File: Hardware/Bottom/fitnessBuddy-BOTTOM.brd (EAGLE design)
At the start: 160 x 100 mm, 31 parts, among them U1 AD5242-SO16

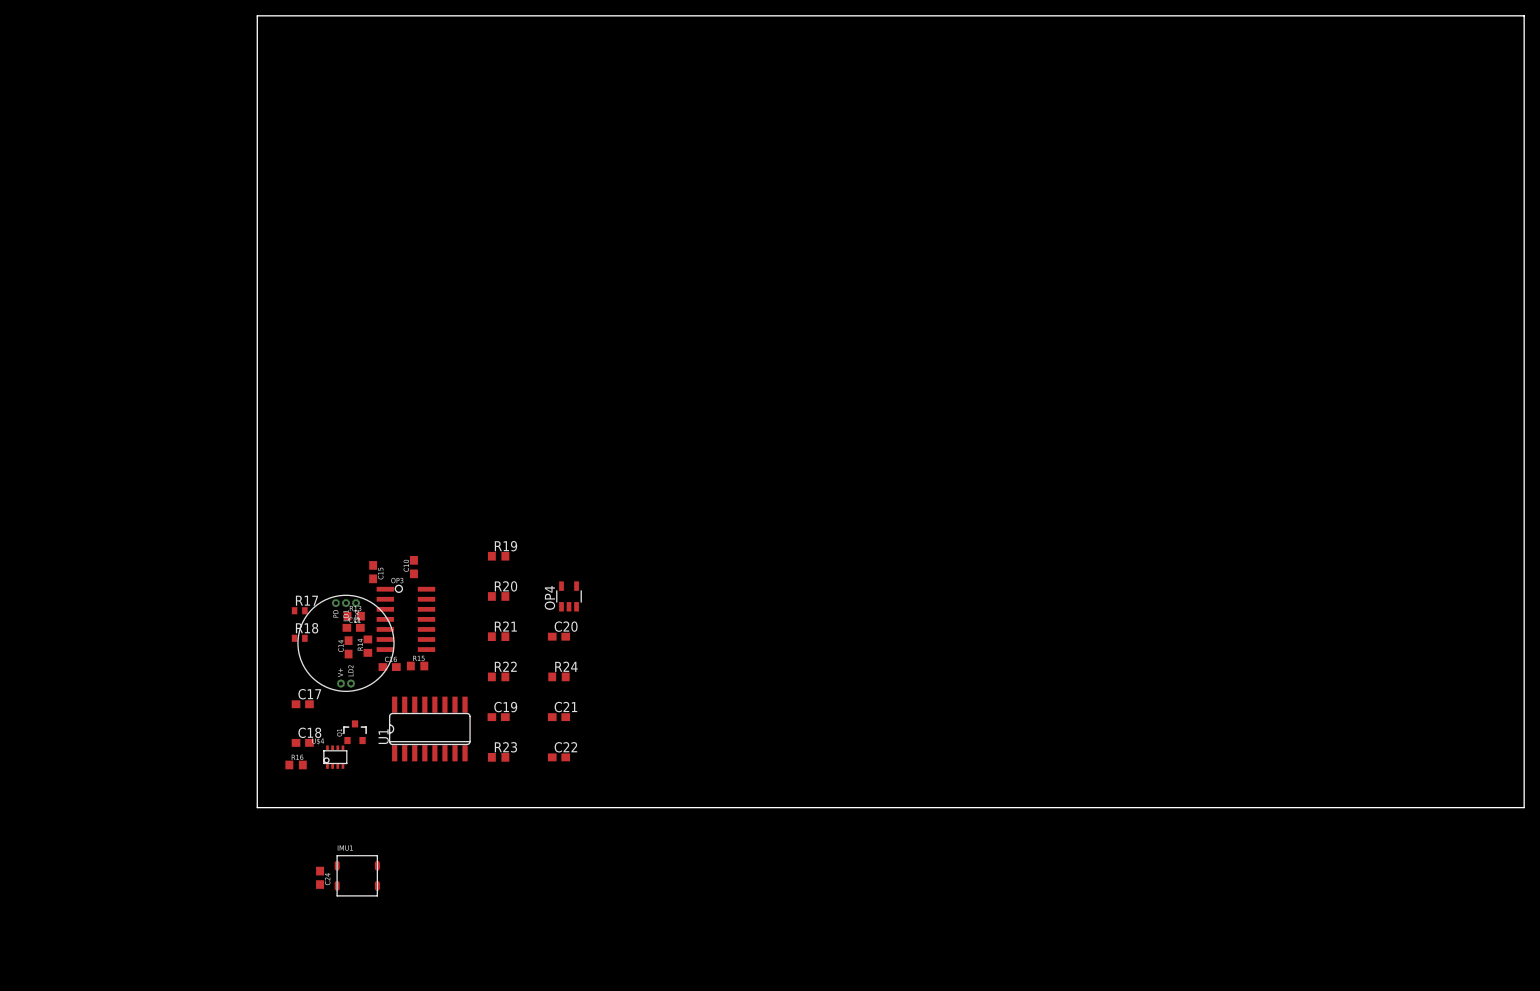
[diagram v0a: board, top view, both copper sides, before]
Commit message: completed adding design blocks to top and bottom boards
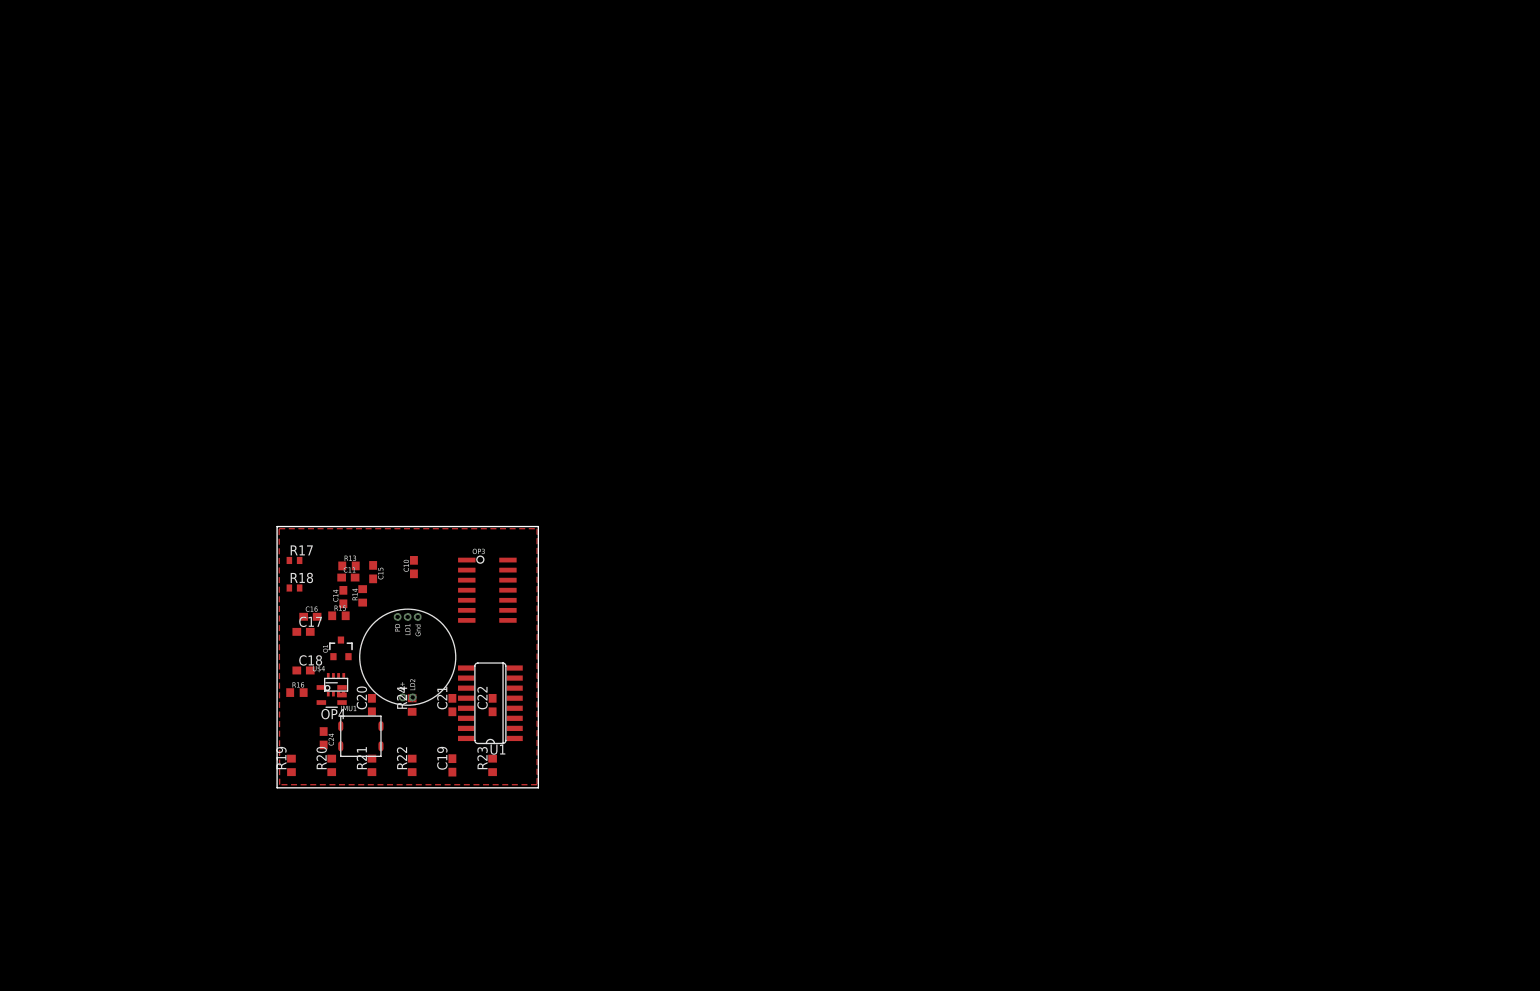
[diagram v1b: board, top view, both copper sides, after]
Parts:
- moved R19 37.2 mm to (4.32, 5.33), turned to 90 degrees
- moved OP4 32.5 mm to (9.40, 14.2), turned to 90 degrees
- moved R20 30.0 mm to (9.40, 5.33), turned to 90 degrees
- moved C20 25.2 mm to (14.5, 13.0), turned to 90 degrees
- moved R21 22.8 mm to (14.5, 5.33), turned to 90 degrees
- moved R24 18.9 mm to (19.6, 13.0), turned to 90 degrees
- moved C24 17.6 mm to (8.38, 8.76)
- moved IMU1 17.6 mm to (13.1, 9.02)
- moved R22 15.6 mm to (19.6, 5.33), turned to 90 degrees
- moved C21 13.5 mm to (24.6, 13.0), turned to 90 degrees
- moved C16 11.9 mm to (6.71, 24.1)
- moved R15 11.8 mm to (10.3, 24.2)
- moved OP3 10.9 mm to (29.1, 27.5)
- moved Q1 10.7 mm to (10.6, 20.1)
- moved C22 10.7 mm to (29.7, 13.0), turned to 90 degrees
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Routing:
- added copper zone on layer 1, net 3.3V
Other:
- board size 160 x 100 mm -> 33 x 33 mm

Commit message: finished bottom board and schematic
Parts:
- added J1: (no value), LinnesLab-Connectors:1X07
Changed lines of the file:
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@@
 <setting verticaltext="up"/>
 </settings>
-<grid distance="1" unitdist="mil" unit="mil" style="lines" multiple="1" display="no" altdistance="5" altunitdist="mil" altunit="mil"/>
+<grid distance="1" unitdist="mil" unit="mm" style="lines" multiple="1" display="no" altdistance="5" altunitdist="mil" altunit="mil"/>
 <layers>
 <layer number="1" name="Top" color="4" fill="1" visible="yes" active="yes"/>
@@
 <attribute name="VALUE" x="6.477" y="9.398" size="0.6604" layer="27" rot="R270"/>
 </element>
+<element name="J1" library="LinnesLab-Connectors" package="1X07" value="" x="5" y="33" smashed="yes">
+<attribute name="NAME" x="3.73" y="34.397" size="0.6096" layer="25" font="vector" ratio="20"/>
+<attribute name="VALUE" x="3.73" y="30.968" size="0.6096" layer="27" font="vector" ratio="20"/>
+</element>
 </elements>
 <signals>
@@
 <contactref element="C24" pad="2"/>
 <polygon width="0.1524" layer="1" isolate="0.1778">
-<vertex x="2.7686" y="35.2298"/>
-<vertex x="35.3314" y="35.2298"/>
-<vertex x="35.3314" y="2.8956"/>
-<vertex x="2.8194" y="2.8956"/>
+<vertex x="3.4318" y="34.5174"/>
+<vertex x="35" y="34.5174"/>
+<vertex x="35" y="3"/>
+<vertex x="3.4318" y="3"/>
 </polygon>
-<wire x1="8.382" y1="7.913" x2="10.541" y2="7.747" width="0" layer="19" extent="1-1"/>
-<wire x1="8.092" y1="13.274" x2="8.382" y2="7.913" width="0" layer="19" extent="1-1"/>
+<wire x1="32.512" y1="15.0876" x2="26.4576" y2="27.4574" width="0" layer="19" extent="1-1"/>
+<wire x1="32.512" y1="13.8176" x2="32.512" y2="15.0876" width="0" layer="19" extent="1-1"/>
+<wire x1="29.718" y1="13.804" x2="32.512" y2="13.8176" width="0" layer="19" extent="1-1"/>
+<wire x1="18.365" y1="13.92" x2="29.718" y2="13.804" width="0" layer="19" extent="1-1"/>
+<wire x1="10.2662" y1="16.6958" x2="18.365" y2="13.92" width="0" layer="19" extent="1-1"/>
+<wire x1="9.6162" y1="14.343" x2="10.2662" y2="16.6958" width="0" layer="19" extent="1-1"/>
+<wire x1="8.092" y1="13.274" x2="9.6162" y2="14.343" width="0" layer="19" extent="1-1"/>
+<wire x1="6.692" y1="17.3228" x2="10.2662" y2="16.6958" width="0" layer="19" extent="1-1"/>
+<wire x1="6.692" y1="22.1996" x2="6.692" y2="17.3228" width="0" layer="19" extent="1-1"/>
+<wire x1="11.1624" y1="24.2316" x2="6.692" y2="22.1996" width="0" layer="19" extent="1-1"/>
+<wire x1="12.3562" y1="29.0576" x2="11.1624" y2="24.2316" width="0" layer="19" extent="1-1"/>
+<wire x1="12.4324" y1="30.5308" x2="12.3562" y2="29.0576" width="0" layer="19" extent="1-1"/>
+<wire x1="8.382" y1="7.913" x2="8.092" y2="13.274" width="0" layer="19" extent="1-1"/>
+<wire x1="10.541" y1="7.747" x2="8.382" y2="7.913" width="0" layer="19" extent="1-1"/>
+<wire x1="5.349" y1="31.2166" x2="12.4324" y2="30.5308" width="0" layer="19" extent="1-1"/>
 </signal>
 <signal name="SDA">

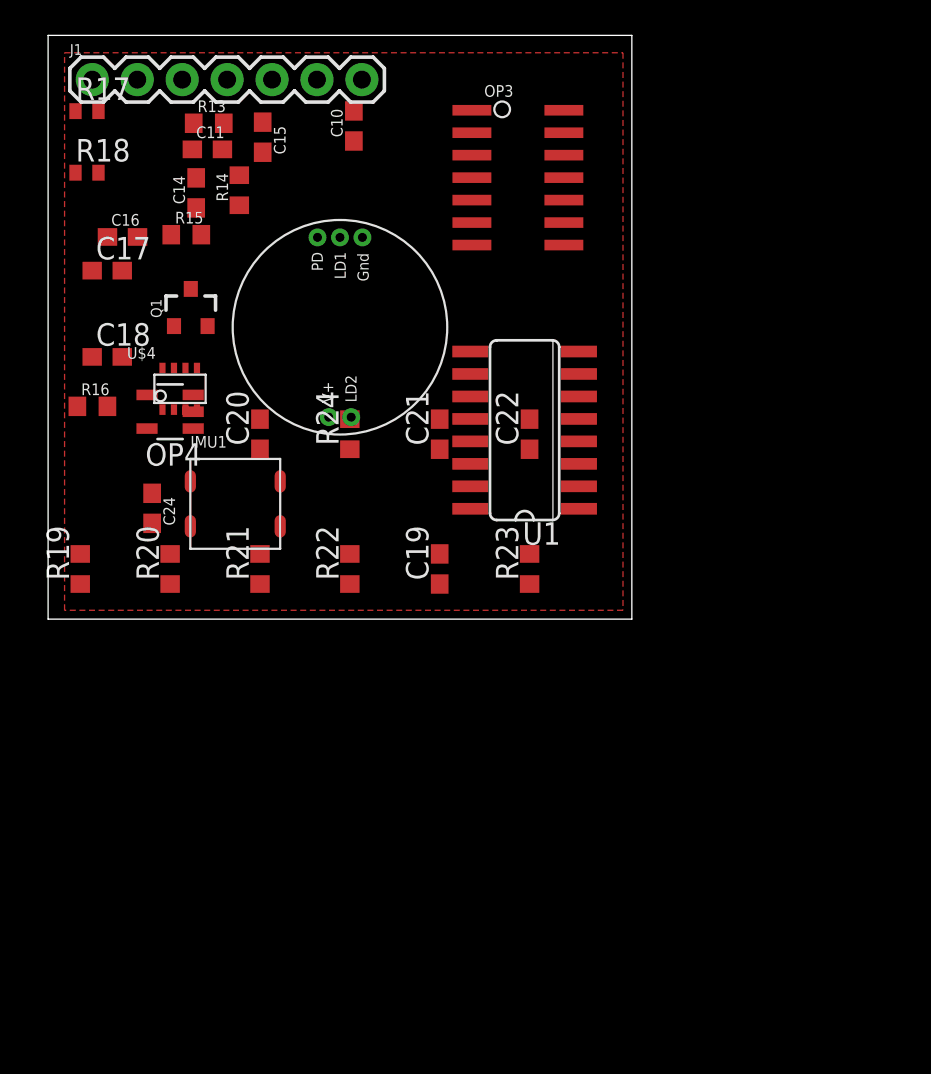
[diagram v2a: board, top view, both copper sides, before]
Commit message: started to route bottom board
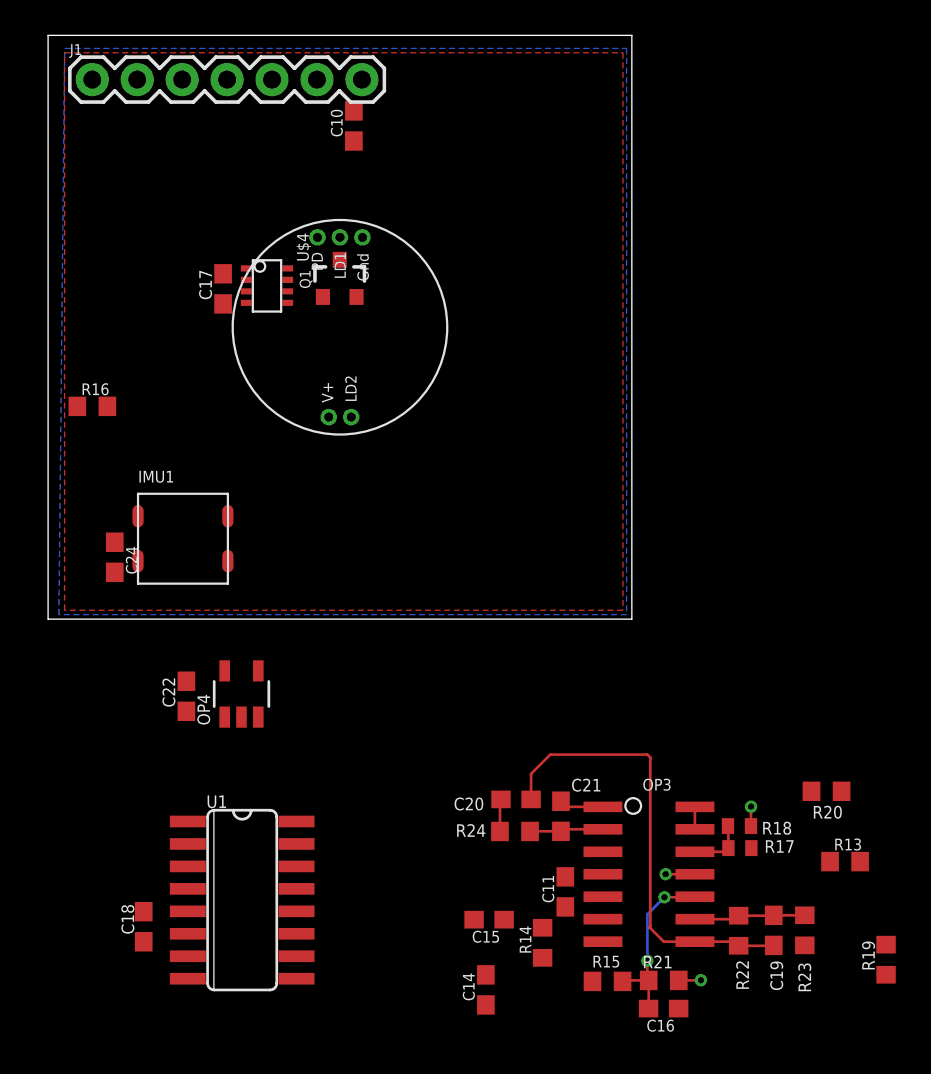
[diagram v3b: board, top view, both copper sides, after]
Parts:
- moved R17 55.7 mm to (41.6, -10.4)
- moved R13 55.1 mm to (47.6, -11.2)
- moved C16 53.3 mm to (37.3, -19.5), turned to 180 degrees
- moved R18 52.2 mm to (41.6, -9.20), turned to 180 degrees
- moved R19 50.6 mm to (49.9, -16.8)
- moved R15 48.5 mm to (34.1, -18.0), turned to 180 degrees
- moved C14 47.9 mm to (27.2, -18.5)
- moved C11 46.6 mm to (31.7, -12.9), turned to 90 degrees
- moved C15 46.0 mm to (27.4, -14.5), turned to 180 degrees
- moved R14 45.9 mm to (30.5, -15.8)
- moved OP3 40.1 mm to (36.5, -11.9)
- moved R20 39.2 mm to (46.5, -7.23), turned to 180 degrees
- moved R21 32.6 mm to (37.3, -17.9), turned to 180 degrees
- moved C18 32.3 mm to (7.90, -14.9), turned to 90 degrees
- moved U1 31.0 mm to (13.5, -13.4), turned to 270 degrees
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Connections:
- net LED.CTRL renamed D29/LED.CTRL
- net PPG renamed A7/PPG
- net TIA renamed A6/TIA
- removed net LED: Q1.3
- new net N$1: J1.7
- new net N$2: J1.6
- new net N$3: J1.5
- net LED.C: now also Q1.3
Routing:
- net N$19: track 0.00 -> 25.8 mm
- net N$17: track 0.00 -> 9.96 mm, vias 0 -> 2
- net N$18: track 0.00 -> 6.30 mm
- net G.W2: track 0.00 -> 4.17 mm
- net GND: track 0.00 -> 4.01 mm, vias 0 -> 3
- net N$10: track 0.00 -> 3.23 mm
- net A7/PPG: track 0.00 -> 2.50 mm
- net N$20: track 0.00 -> 1.84 mm
- net VREF: track 0.00 -> 1.27 mm
- added copper zone on layer 16, net GND

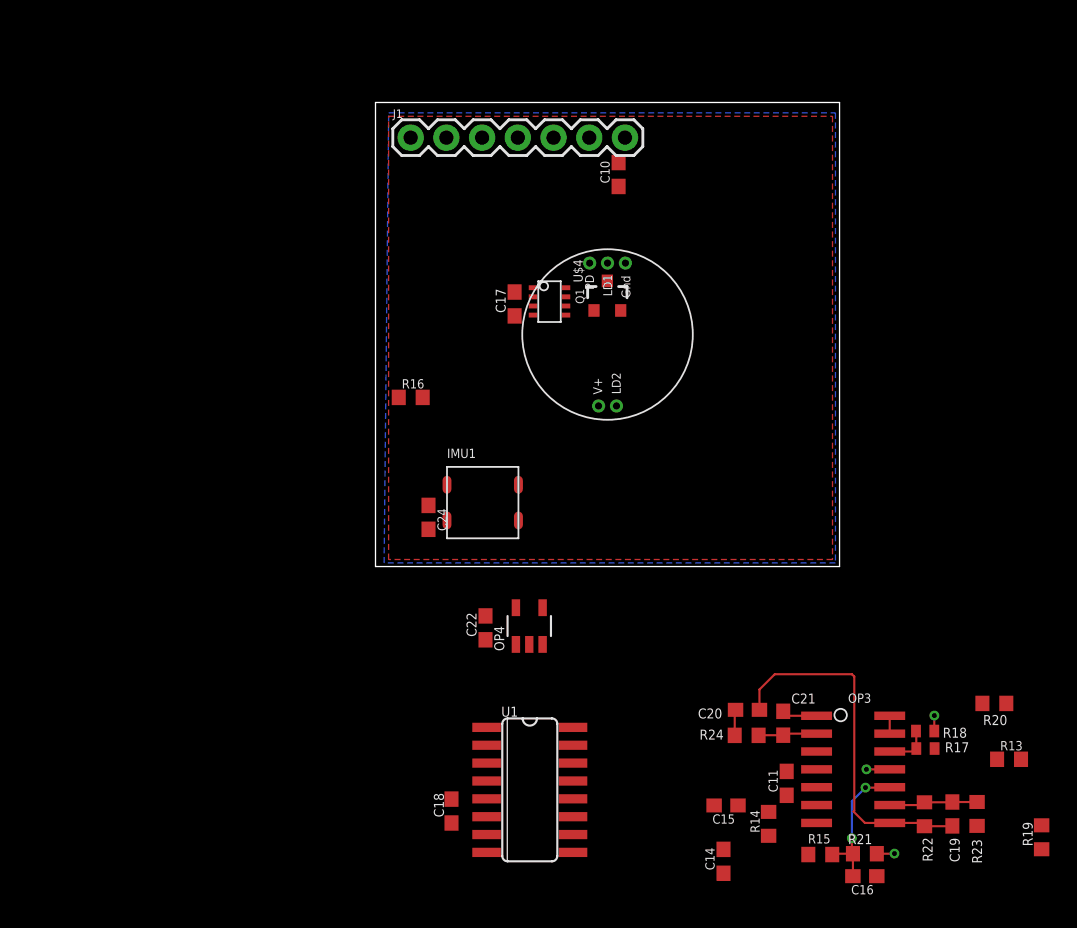
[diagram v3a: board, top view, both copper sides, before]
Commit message: Made progress on routing bottom board
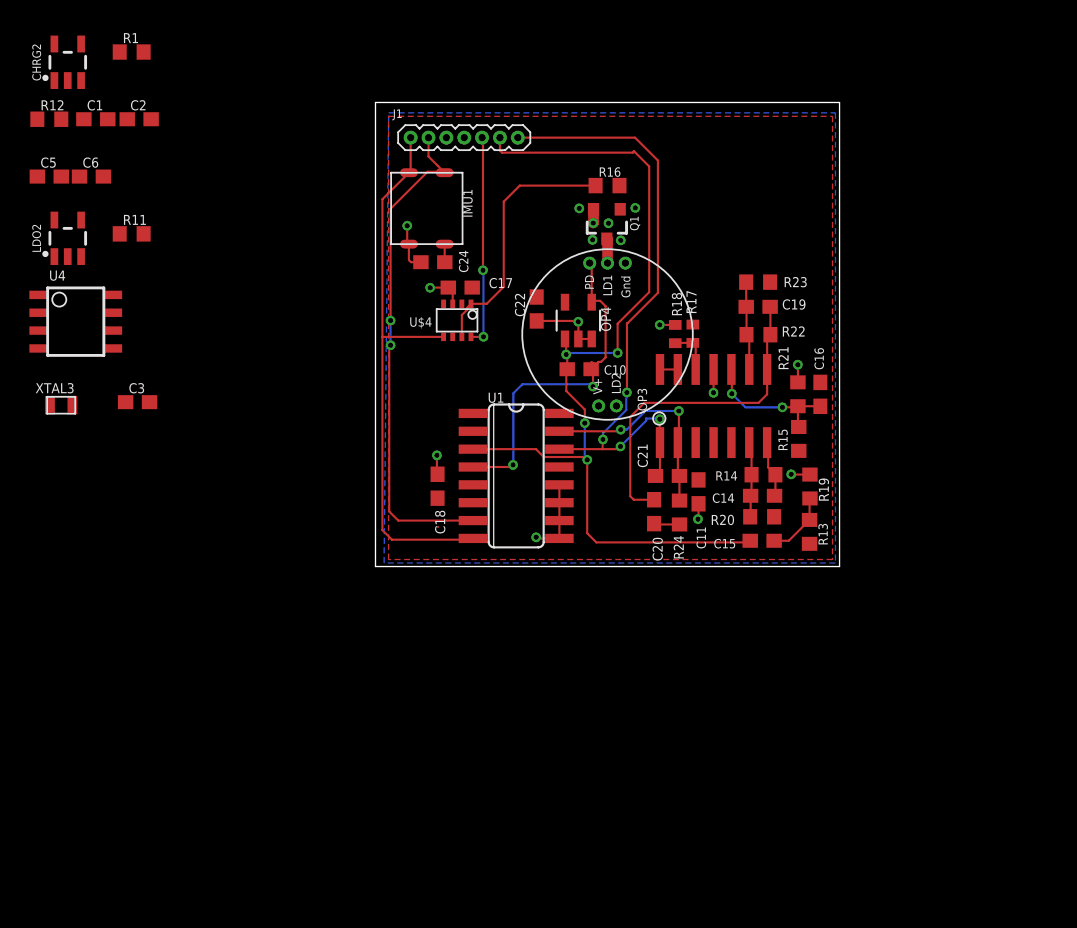
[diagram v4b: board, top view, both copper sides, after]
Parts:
- added C1, C2: 4.7u, LinnesLab-Passives:C0603
- added C3, C5, C6: 1u, LinnesLab-Passives:C0603
- added CHRG2: MCP73831, LinnesLab-Power:SOT23-5
- added LDO2: MIC5504, LinnesLab-Power:SOT23-5
- added R1, R12: 100k, LinnesLab-Passives:R0603
- added R11: (no value), LinnesLab-Passives:R0603
- added U4: PCF8523, LinnesLab-Clocks:SO8
- added XTAL3: 32.7680kHz, LinnesLab-Clocks:2-SMD.NOLEAD.2.0MMTO1.2MM
- J1: device LinnesLab-Connectors:1X07 -> LinnesLab-Connectors:1X07_1.27MM
- moved R23 40.9 mm to (29.7, 22.7), turned to 180 degrees
- moved C19 38.6 mm to (29.7, 21.0), turned to 180 degrees
- moved R22 36.1 mm to (29.7, 19.0), turned to 0 degrees
- moved C16 34.4 mm to (34.1, 14.7), turned to 270 degrees
- moved R17 33.8 mm to (25.1, 19.1), turned to 90 degrees
- moved R18 33.4 mm to (23.8, 19.0), turned to 270 degrees
- moved R21 33.0 mm to (32.5, 14.7), turned to 270 degrees
- moved R19 29.9 mm to (33.4, 8.19), turned to 270 degrees
- moved R15 29.6 mm to (32.6, 11.6), turned to 270 degrees
- moved OP3 27.7 mm to (26.5, 13.9), turned to 0 degrees
- moved C14 26.1 mm to (30.0, 7.53), turned to 180 degrees
- moved R14 24.8 mm to (30.1, 9.03), turned to 0 degrees
- moved C18 23.1 mm to (6.91, 8.21), turned to 270 degrees
- moved C22 23.0 mm to (14.0, 20.8)
- moved U1 22.3 mm to (12.5, 8.94)
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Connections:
- removed net N$1: J1.7
- removed net N$2: J1.6
- removed net N$3: J1.5
- new net D27/CHRG.STATUS: CHRG2.1, R12.1
- new net N$4: CHRG2.5, R11.2
- new net N$5: U4.2, XTAL3.P$1
- new net N$6: U4.1, XTAL3.P$2
- new net VBATT: U4.3
- new net VIN: C2.2, C5.2, CHRG2.4, LDO2.1, LDO2.3, R12.2
- new net VLIPO: C1.1, CHRG2.3
- net 3.3V: now also C3.1, C6.1, J1.4, LDO2.5, R1.2, U4.8
- net A6/TIA: now also J1.6
- net A7/PPG: now also J1.7
- net D29/LED.CTRL: now also J1.5
- net GND: now also C1.2, C2.1, C3.2, C5.1, C6.2, CHRG2.2, J1.3, LDO2.2, R1.1, R11.1, U4.4
- net SCL: now also J1.2, U4.6
- net SDA: now also J1.1, U4.5
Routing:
- net A6/TIA: track 0.00 -> 64.9 mm, vias 0 -> 4
- net A7/PPG: track 2.50 -> 45.4 mm, vias 0 -> 4
- net SDA: track 0.00 -> 39.9 mm
- net SCL: track 0.00 -> 35.6 mm, vias 0 -> 2
- net PD.C: track 0.00 -> 24.8 mm, vias 0 -> 2
- net GND: track 4.01 -> 25.7 mm, vias 3 -> 14
- net N$9: track 0.00 -> 18.5 mm
- net D29/LED.CTRL: track 0.00 -> 15.1 mm, vias 0 -> 2
- net G.W2: track 4.17 -> 15.7 mm, vias 0 -> 2
- net N$15: track 0.00 -> 5.38 mm
- net N$13: track 0.00 -> 4.67 mm
- net N$16: track 0.00 -> 4.05 mm
- net LED.C: track 0.00 -> 1.74 mm
- net N$19: track 25.8 -> 24.2 mm
- net 3.3V: track 0.00 -> 1.32 mm
